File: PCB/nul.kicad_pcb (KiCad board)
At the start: 4 copper layers, 11 x 43.2 mm, 30 parts, among them J2 LED Socket, U1 ESP32-C3FH4, U2 AMS1117-3.3, U3 SN74AHCT1G125DBVR, U4 XRCGB40M000F1S1DR0, U5 SRV05-4

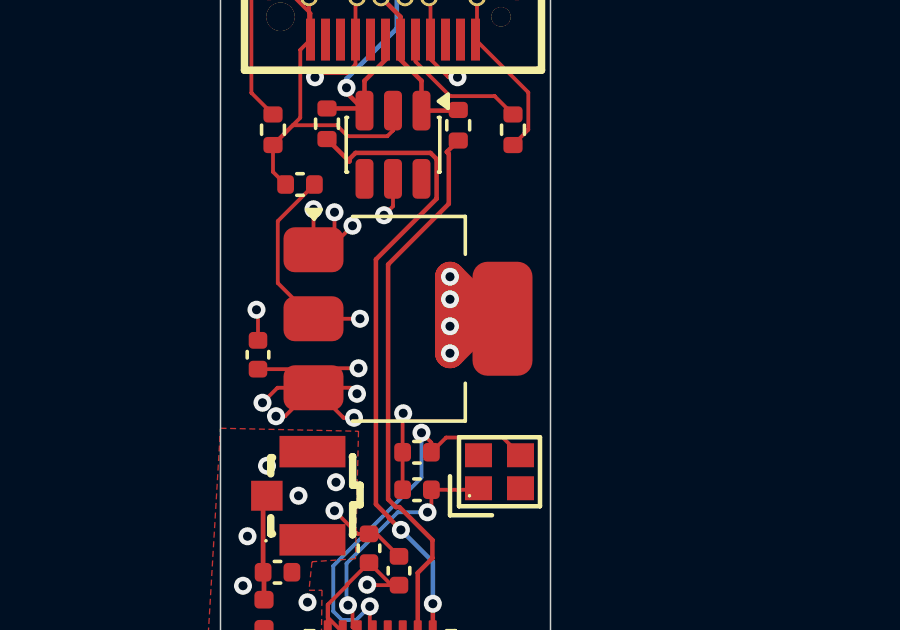
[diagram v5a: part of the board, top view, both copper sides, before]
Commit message: update parallel traces
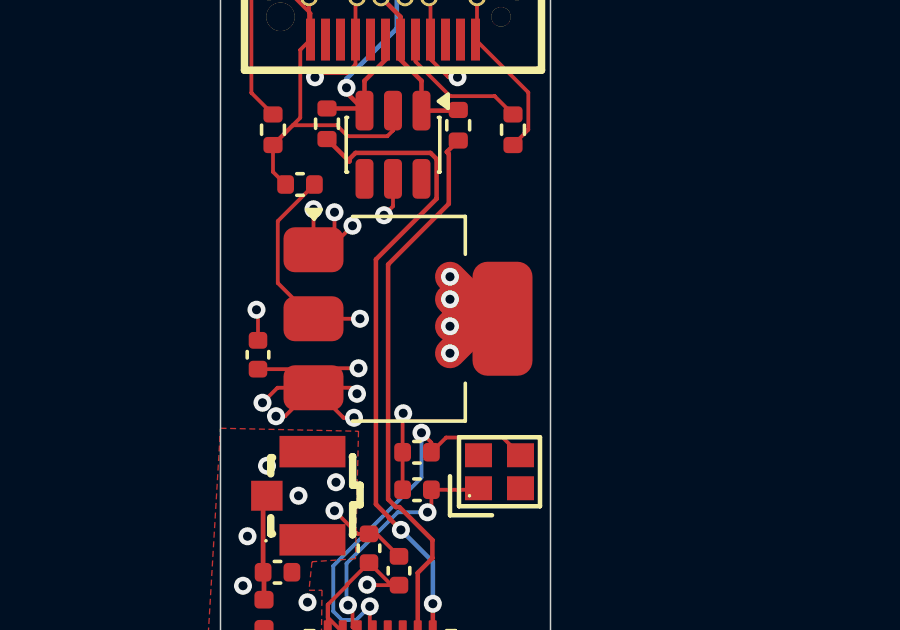
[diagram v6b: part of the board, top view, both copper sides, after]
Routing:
- net +3.3V: track 79.5 -> 75.9 mm
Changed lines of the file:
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@@
-	)
-	(segment
-		(start 121.9 55.9)
-		(end 121.9 58.45)
-		(width 1)
-		(layer "F.Cu")
-		(net "+3.3V")
 	)
 	(segment
@@
 	)
 	(segment
-		(start 120.05 58.45)
-		(end 121.9 58.45)
-		(width 0.254)
-		(layer "In2.Cu")
-		(net "+3.3V")
-	)
-	(segment
-		(start 121.9 63.45)
-		(end 121.9 56.95)
+		(start 121.9 58.45)
+		(end 121.9 55.9)
+		(width 1)
+		(layer "In2.Cu")
+		(net "+3.3V")
+	)
+	(segment
+		(start 117.946 71.904)
+		(end 115.6 74.25)
+		(width 0.254)
+		(layer "In2.Cu")
+		(net "+3.3V")
+	)
+	(segment
+		(start 118.400057 66.166468)
+		(end 117.946 66.620525)
 		(width 0.254)
 		(layer "In2.Cu")
@@
 	)
 	(segment
-		(start 117.15 71.8)
-		(end 121.9 67.05)
-		(width 0.254)
-		(layer "In2.Cu")
-		(net "+3.3V")
-	)
-	(segment
-		(start 120.3 55.9)
-		(end 118.9 57.3)
-		(width 0.254)
-		(layer "In2.Cu")
-		(net "+3.3V")
-	)
-	(segment
-		(start 121.583532 66.166468)
-		(end 121.9 65.85)
-		(width 0.127)
-		(layer "In2.Cu")
-		(net "+3.3V")
-	)
-	(segment
-		(start 121.9 67.05)
-		(end 121.9 65.85)
-		(width 0.254)
-		(layer "In2.Cu")
-		(net "+3.3V")
-	)
-	(segment
-		(start 121.9 65.85)
-		(end 121.9 63.45)
+		(start 121.9 55.9)
+		(end 121.9 65.05)
+		(width 0.254)
+		(layer "In2.Cu")
+		(net "+3.3V")
+	)
+	(segment
+		(start 118.9 57.3)
+		(end 120.75 57.3)
+		(width 1)
+		(layer "In2.Cu")
+		(net "+3.3V")
+	)
+	(segment
+		(start 120.5 57.3)
+		(end 121.9 55.9)
+		(width 1)
+		(layer "In2.Cu")
+		(net "+3.3V")
+	)
+	(segment
+		(start 121.9 65.05)
+		(end 120.783532 66.166468)
+		(width 0.254)
+		(layer "In2.Cu")
+		(net "+3.3V")
+	)
+	(segment
+		(start 120.783532 66.166468)
+		(end 119.140057 66.166468)
+		(width 0.254)
+		(layer "In2.Cu")
+		(net "+3.3V")
+	)
+	(segment
+		(start 119.140057 66.166468)
+		(end 118.400057 66.166468)
 		(width 0.254)
 		(layer "In2.Cu")
@@
 		(start 118.9 57.3)
 		(end 121.65 57.3)
+		(width 1)
+		(layer "In2.Cu")
+		(net "+3.3V")
+	)
+	(segment
+		(start 118.9 57.3)
+		(end 120.5 57.3)
+		(width 1)
+		(layer "In2.Cu")
+		(net "+3.3V")
+	)
+	(segment
+		(start 120.75 57.3)
+		(end 121.9 58.45)
+		(width 1)
+		(layer "In2.Cu")
+		(net "+3.3V")
+	)
+	(segment
+		(start 117.946 66.620525)
+		(end 117.946 71.904)
 		(width 0.254)
 		(layer "In2.Cu")
@@
 		(start 121.65 57.3)
 		(end 121.9 57.55)
-		(width 0.254)
-		(layer "In2.Cu")
-		(net "+3.3V")
-	)
-	(segment
-		(start 121.9 55.9)
-		(end 120.3 55.9)
-		(width 0.254)
-		(layer "In2.Cu")
-		(net "+3.3V")
-	)
-	(segment
-		(start 115.6 74.25)
-		(end 117.15 72.7)
-		(width 0.254)
-		(layer "In2.Cu")
-		(net "+3.3V")
-	)
-	(segment
-		(start 117.15 72.7)
-		(end 117.15 71.8)
-		(width 0.254)
-		(layer "In2.Cu")
-		(net "+3.3V")
-	)
-	(segment
-		(start 119.25 56.95)
-		(end 118.9 57.3)
-		(width 0.254)
-		(layer "In2.Cu")
-		(net "+3.3V")
-	)
-	(segment
-		(start 121.9 56.95)
-		(end 119.25 56.95)
-		(width 0.254)
-		(layer "In2.Cu")
-		(net "+3.3V")
-	)
-	(segment
-		(start 118.9 57.3)
-		(end 120.05 58.45)
-		(width 0.254)
-		(layer "In2.Cu")
-		(net "+3.3V")
-	)
-	(segment
-		(start 119.140057 66.166468)
-		(end 121.583532 66.166468)
-		(width 0.127)
-		(layer "In2.Cu")
-		(net "+3.3V")
+		(width 1)
+		(layer "In2.Cu")
+		(net "+3.3V")

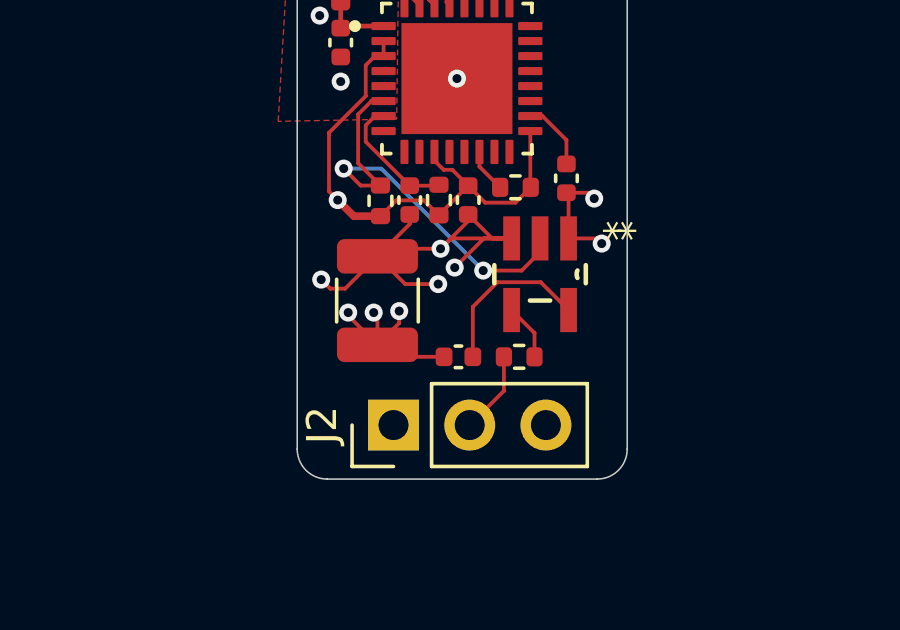
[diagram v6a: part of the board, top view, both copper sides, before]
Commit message: fix level shifter decoupling capacitor
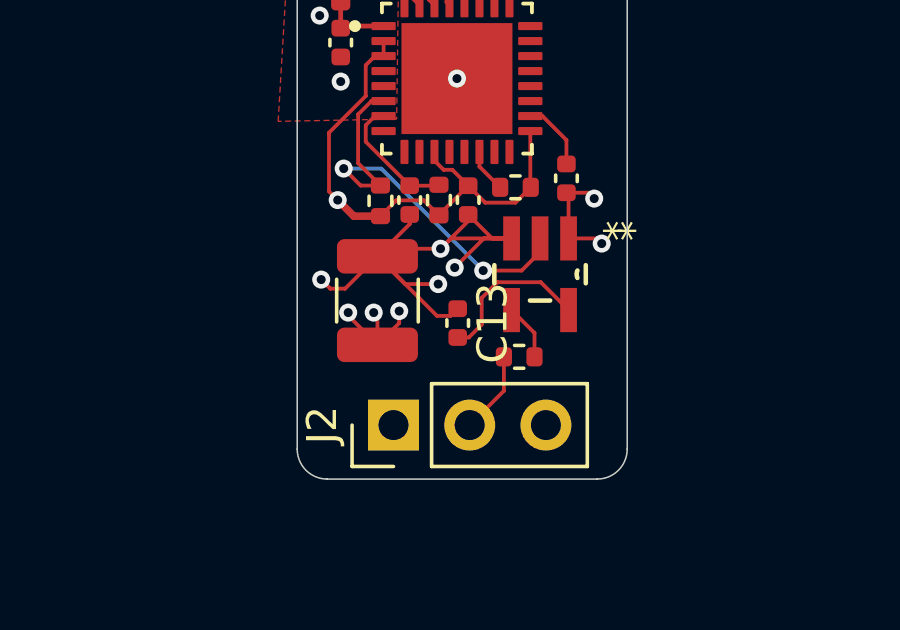
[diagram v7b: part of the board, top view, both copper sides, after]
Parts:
- C13: value 0.1uF -> 0.1uF ceramic
- moved C13 1.13 mm to (119.6, 78.3), turned to -90 degrees
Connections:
- C13 pad 1: +5V -> GND
- C13 pad 2: Net-(U3-VCC) -> +5V
- U3 pad 5: Net-(U3-VCC) -> +5V
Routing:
- net Net-(U3-VCC): track 5.58 -> 0.00 mm
- net GND: track 55.5 -> 59.1 mm
- net +5V: track 25.5 -> 29.0 mm
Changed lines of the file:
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@@
 	(footprint "Capacitor_SMD:C_0402_1005Metric"
 		(layer "F.Cu")
+		(at 119.6 78.35 -90)
+		(descr "Capacitor SMD 0402 (1005 Metric), square (rectangular) end terminal, IPC-7351 nominal, (Body size source: IPC-SM-782 page 76, https://www.pcb-3d.com/wordpress/wp-content/uploads/ipc-sm-782a_amendment_1_and_2.pdf)")
+		(tags "capacitor")
+		(property "Reference" "C13"
+			(at 0 -1.16 90)
+			(layer "F.SilkS")
+			(effects
+				(font
+					(size 1 1)
+					(thickness 0.15)
+				)
+			)
+		)
+		(property "Value" "0.1uF ceramic"
+			(at 0 1.16 90)
+			(layer "F.Fab")
+			(effects
+				(font
+					(size 1 1)
+					(thickness 0.15)
+				)
+			)
+		)
+		(property "Datasheet" ""
+			(at 0 0 90)
+			(layer "F.Fab")
+			(hide yes)
+			(effects
+				(font
+					(size 1.27 1.27)
+				)
+			)
+		)
+		(property "Description" "Unpolarized capacitor, small symbol"
+			(at 0 0 90)
+			(layer "F.Fab")
+			(hide yes)
+			(effects
+				(font
+					(size 1.27 1.27)
+				)
+			)
+		)
+		(property "KiLib_Generator" "SMD_2terminal_chip_molded"
+			(at 0 0 90)
+			(layer "F.SilkS")
+			(hide yes)
+			(effects
+				(font
+					(size 1 1)
+					(thickness 0.15)
+				)
+			)
+		)
+		(property "LCSC Part" "C1525"
+			(at 0 0 270)
+			(unlocked yes)
+			(layer "F.Fab")
+			(hide yes)
+			(effects
+				(font
+					(size 1 1)
+					(thickness 0.15)
+				)
+			)
+		)
+		(property ki_fp_filters "C_*")
+		(sheetname "/")
+		(sheetfile "nul.kicad_sch")
+		(units
+			(unit
+				(name "A")
+				(pins "1" "2")
+			)
+		)
+		(attr smd)
+		(duplicate_pad_numbers_are_jumpers no)
+		(fp_line
+			(start -0.107836 0.36)
+			(end 0.107836 0.36)
+			(stroke
+				(width 0.12)
+				(type solid)
+			)
+			(layer "F.SilkS")
+		)
+		(fp_line
+			(start -0.107836 -0.36)
+			(end 0.107836 -0.36)
+			(stroke
+				(width 0.12)
+				(type solid)
+			)
+			(layer "F.SilkS")
+		)
+		(fp_rect
+			(start -0.91 -0.46)
+			(end 0.91 0.46)
+			(stroke
+				(width 0.05)
+				(type solid)
+			)
+			(fill no)
+			(layer "F.CrtYd")
+		)
+		(fp_rect
+			(start -0.5 -0.25)
+			(end 0.5 0.25)
+			(stroke
+				(width 0.1)
+				(type solid)
+			)
+			(fill no)
+			(layer "F.Fab")
+		)
+		(fp_text user "${REFERENCE}"
+			(at 0 0 90)
+			(layer "F.Fab")
+			(effects
+				(font
+					(size 0.25 0.25)
+					(thickness 0.04)
+				)
+			)
+		)
+		(pad "1" smd roundrect
+			(at -0.48 0 270)
+			(size 0.56 0.62)
+			(layers "F.Cu" "F.Mask" "F.Paste")
+			(roundrect_rratio 0.25)
+			(net "GND")
+			(pintype "passive")
+		)
+		(pad "2" smd roundrect
+			(at 0.48 0 270)
+			(size 0.56 0.62)
+			(layers "F.Cu" "F.Mask" "F.Paste")
+			(roundrect_rratio 0.25)
+			(net "+5V")
+			(pintype "passive")
+		)
+		(embedded_fonts no)
+		(model "${KICAD10_3DMODEL_DIR}/Capacitor_SMD.3dshapes/C_0402_1005Metric.step"
+			(offset
+				(xyz 0 0 0)
+			)
+			(scale
+				(xyz 1 1 1)
+			)
+			(rotate
+				(xyz 0 0 0)
+			)
+		)
+	)
+	(footprint "Capacitor_SMD:C_0402_1005Metric"
+		(layer "F.Cu")
 		(at 120.8 61.75 180)
 		(descr "Capacitor SMD 0402 (1005 Metric), square (rectangular) end terminal, IPC-7351 nominal, (Body size source: IPC-SM-782 page 76, https://www.pcb-3d.com/wordpress/wp-content/uploads/ipc-sm-782a_amendment_1_and_2.pdf)")
@@
 			(size 1.4732 0.5588)
 			(layers "F.Cu" "F.Mask" "F.Paste")
-			(net "Net-(U3-VCC)")
+			(net "+5V")
 			(pinfunction "VCC_5")
 			(pintype "power_in")
@@
 		)
 	)
-	(footprint "Capacitor_SMD:C_0402_1005Metric"
-		(layer "F.Cu")
-		(at 119.625 79.475)
-		(descr "Capacitor SMD 0402 (1005 Metric), square (rectangular) end terminal, IPC-7351 nominal, (Body size source: IPC-SM-782 page 76, https://www.pcb-3d.com/wordpress/wp-content/uploads/ipc-sm-782a_amendment_1_and_2.pdf)")
-		(tags "capacitor")
-		(property "Reference" "C13"
-			(at 0 -1.16 0)
-			(layer "F.SilkS")
-			(hide yes)
-			(effects
-				(font
-					(size 1 1)
-					(thickness 0.15)
-				)
-			)
-		)
-		(property "Value" "0.1uF"
-			(at 0 1.16 0)
-			(layer "F.Fab")
-			(effects
-				(font
-					(size 1 1)
-					(thickness 0.15)
-				)
-			)
-		)
-		(property "Datasheet" ""
-			(at 0 0 0)
-			(layer "F.Fab")
-			(hide yes)
-			(effects
-				(font
-					(size 1.27 1.27)
-				)
-			)
-		)
-		(property "Description" "Unpolarized capacitor"
-			(at 0 0 0)
-			(layer "F.Fab")
-			(hide yes)
-			(effects
-				(font
-					(size 1.27 1.27)
-				)
-			)
-		)
-		(property "LCSC Part" "C1525"
-			(at 0 0 0)
-			(unlocked yes)
-			(layer "F.Fab")
-			(hide yes)
-			(effects
-				(font
-					(size 1 1)
-					(thickness 0.15)
-				)
-			)
-		)
-		(property ki_fp_filters "C_*")
-		(sheetname "/")
-		(sheetfile "nul.kicad_sch")
-		(units
-			(unit
-				(name "A")
-				(pins "1" "2")
-			)
-		)
-		(attr smd)
-		(duplicate_pad_numbers_are_jumpers no)
-		(fp_line
-			(start -0.107836 -0.36)
-			(end 0.107836 -0.36)
-			(stroke
-				(width 0.12)
-				(type solid)
-			)
-			(layer "F.SilkS")
-		)
-		(fp_line
-			(start -0.107836 0.36)
-			(end 0.107836 0.36)
-			(stroke
-				(width 0.12)
-				(type solid)
-			)
-			(layer "F.SilkS")
-		)
-		(fp_rect
-			(start -0.91 -0.46)
-			(end 0.91 0.46)
-			(stroke
-				(width 0.05)
-				(type solid)
-			)
-			(fill no)
-			(layer "F.CrtYd")
-		)
-		(fp_rect
-			(start -0.5 -0.25)
-			(end 0.5 0.25)
-			(stroke
-				(width 0.1)
-				(type solid)
-			)
-			(fill no)
-			(layer "F.Fab")
-		)
-		(fp_text user "${REFERENCE}"
-			(at 0 0 0)
-			(layer "F.Fab")
-			(effects
-				(font
-					(size 0.25 0.25)
-					(thickness 0.04)
-				)
-			)
-		)
-		(pad "1" smd roundrect
-			(at -0.48 0)
-			(size 0.56 0.62)
-			(layers "F.Cu" "F.Mask" "F.Paste")
-			(roundrect_rratio 0.25)
-			(net "+5V")
-			(pintype "passive")
-		)
-		(pad "2" smd roundrect
-			(at 0.48 0)
-			(size 0.56 0.62)
-			(layers "F.Cu" "F.Mask" "F.Paste")
-			(roundrect_rratio 0.25)
-			(net "Net-(U3-VCC)")
-			(pintype "passive")
-		)
-		(embedded_fonts no)
-		(model "${KICAD10_3DMODEL_DIR}/Capacitor_SMD.3dshapes/C_0402_1005Metric.step"
-			(offset
-				(xyz 0 0 0)
-			)
-			(scale
-				(xyz 1 1 1)
-			)
-			(rotate
-				(xyz 0 0 0)
-			)
-		)
-	)
 	(footprint "Resistor_SMD:R_0402_1005Metric"
 		(layer "F.Cu")
@@
 	)
 	(segment
+		(start 118.9105 78.1105)
+		(end 116.925 76.125)
+		(width 0.127)
+		(layer "F.Cu")
+		(net "GND")
+	)
+	(segment
 		(start 117.85 55)
 		(end 118.65 54.2)
@@
 	)
 	(segment
+		(start 119.6 77.87)
+		(end 119.3595 78.1105)
+		(width 0.127)
+		(layer "F.Cu")
+		(net "GND")
+	)
+	(segment
 		(start 121.395302 75.527951)
 		(end 120.747951 75.527951)
@@
 	)
 	(segment
+		(start 119.3595 78.1105)
+		(end 118.9105 78.1105)
+		(width 0.127)
+		(layer "F.Cu")
+		(net "GND")
+	)
+	(segment
 		(start 116.925 76.125)
 		(end 117.85 77.05)
@@
 	)
 	(segment
-		(start 117.35 59.6)
-		(end 116.4 60.55)
+		(start 122.368204 76.988451)
+		(end 120.925402 76.988451)
 		(width 0.127)
 		(layer "F.Cu")
@@
 	)
 	(segment
-		(start 117.325 79.475)
-		(end 116.925 79.075)
+		(start 117.35 59.6)
+		(end 116.4 60.55)
 		(width 0.127)
 		(layer "F.Cu")
@@
 	)
 	(segment
-		(start 119.145 79.475)
-		(end 117.325 79.475)
+		(start 117.325 79.475)
+		(end 116.925 79.075)
 		(width 0.127)
 		(layer "F.Cu")
@@
 	)
 	(segment
+		(start 120.4 77.513853)
+		(end 120.4 78.4)
+		(width 0.127)
+		(layer "F.Cu")
+		(net "+5V")
+	)
+	(segment
 		(start 120 53.55)
 		(end 119.7 53.85)
@@
 	)
 	(segment
+		(start 119.97 78.83)
+		(end 119.6 78.83)
+		(width 0.127)
+		(layer "F.Cu")
+		(net "+5V")
+	)
+	(segment
 		(start 118.6 59.6)
 		(end 118.8 59.8)
@@
 	)
 	(segment
+		(start 123.295304 77.915551)
+		(end 122.368204 76.988451)
+		(width 0.127)
+		(layer "F.Cu")
+		(net "+5V")
+	)
+	(segment
 		(start 121.25 48.65)
 		(end 121.85 49.25)
@@
 	)
 	(segment
+		(start 120.4 78.4)
+		(end 119.97 78.83)
+		(width 0.127)
+		(layer "F.Cu")
+		(net "+5V")
+	)
+	(segment
 		(start 117.35 59.6)
 		(end 118 58.95)
@@
 	)
 	(segment
+		(start 120.925402 76.988451)
+		(end 120.4 77.513853)
+		(width 0.127)
+		(layer "F.Cu")
+		(net "+5V")
+	)
+	(segment
 		(start 121.25 47.995)
 		(end 121.25 46.635)
@@
 	)
 	(segment
-		(start 120.105 77.808853)
-		(end 120.105 79.475)
-		(width 0.127)
-		(layer "F.Cu")
-		(net "Net-(U3-VCC)")
-	)
-	(segment
-		(start 120.925402 76.988451)
-		(end 120.105 77.808853)
-		(width 0.127)
-		(layer "F.Cu")
-		(net "Net-(U3-VCC)")
-	)
-	(segment
-		(start 122.368204 76.988451)
-		(end 120.925402 76.988451)
-		(width 0.127)
-		(layer "F.Cu")
-		(net "Net-(U3-VCC)")
-	)
-	(segment
-		(start 123.295304 77.915551)
-		(end 122.368204 76.988451)
-		(width 0.127)
-		(layer "F.Cu")
-		(net "Net-(U3-VCC)")
-	)
-	(segment
